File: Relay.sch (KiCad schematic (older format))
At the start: 11 parts

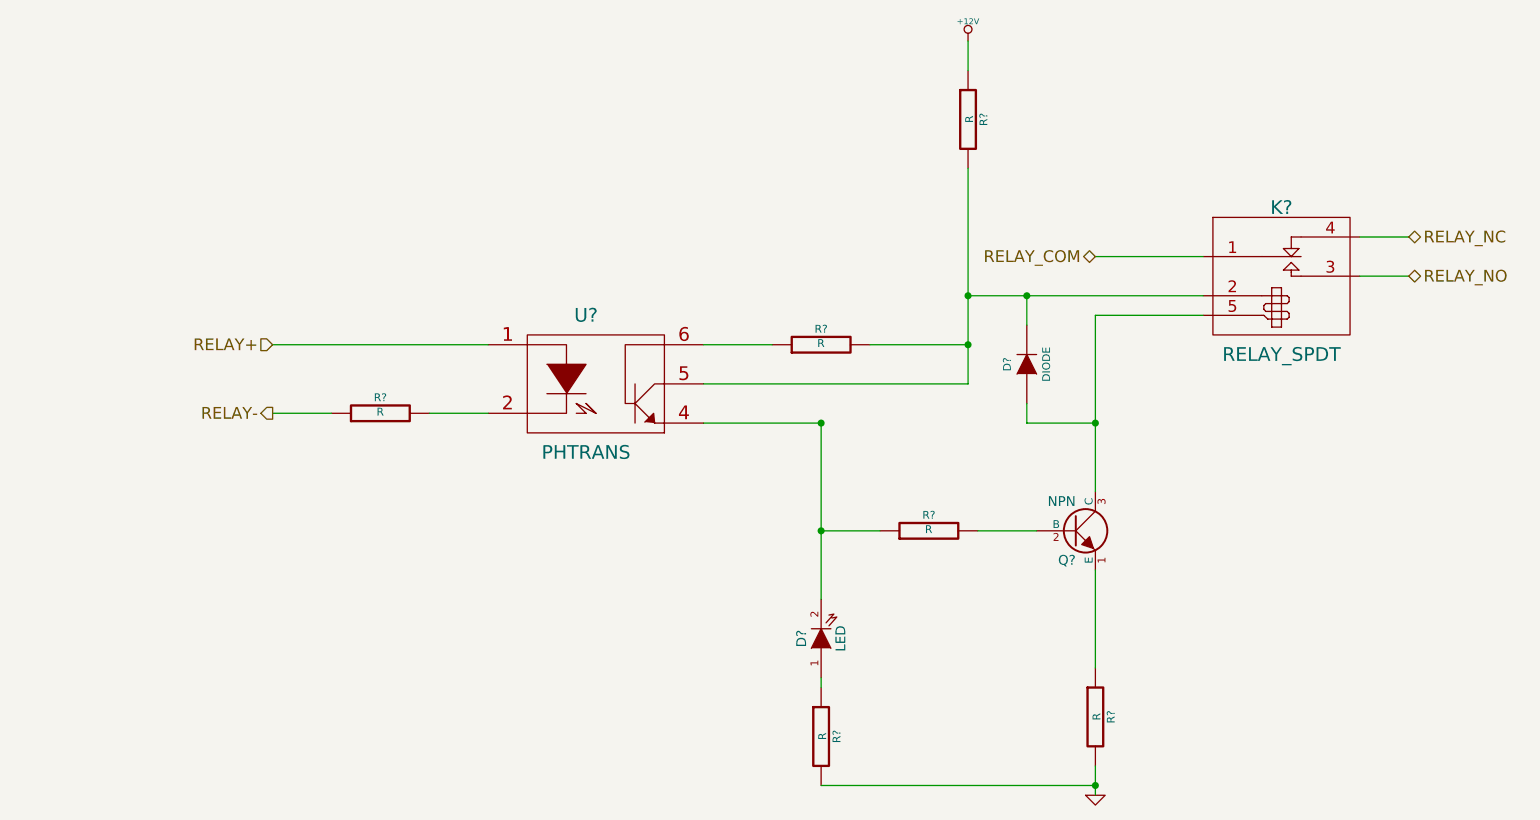
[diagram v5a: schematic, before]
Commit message: Begin Associating relay Module
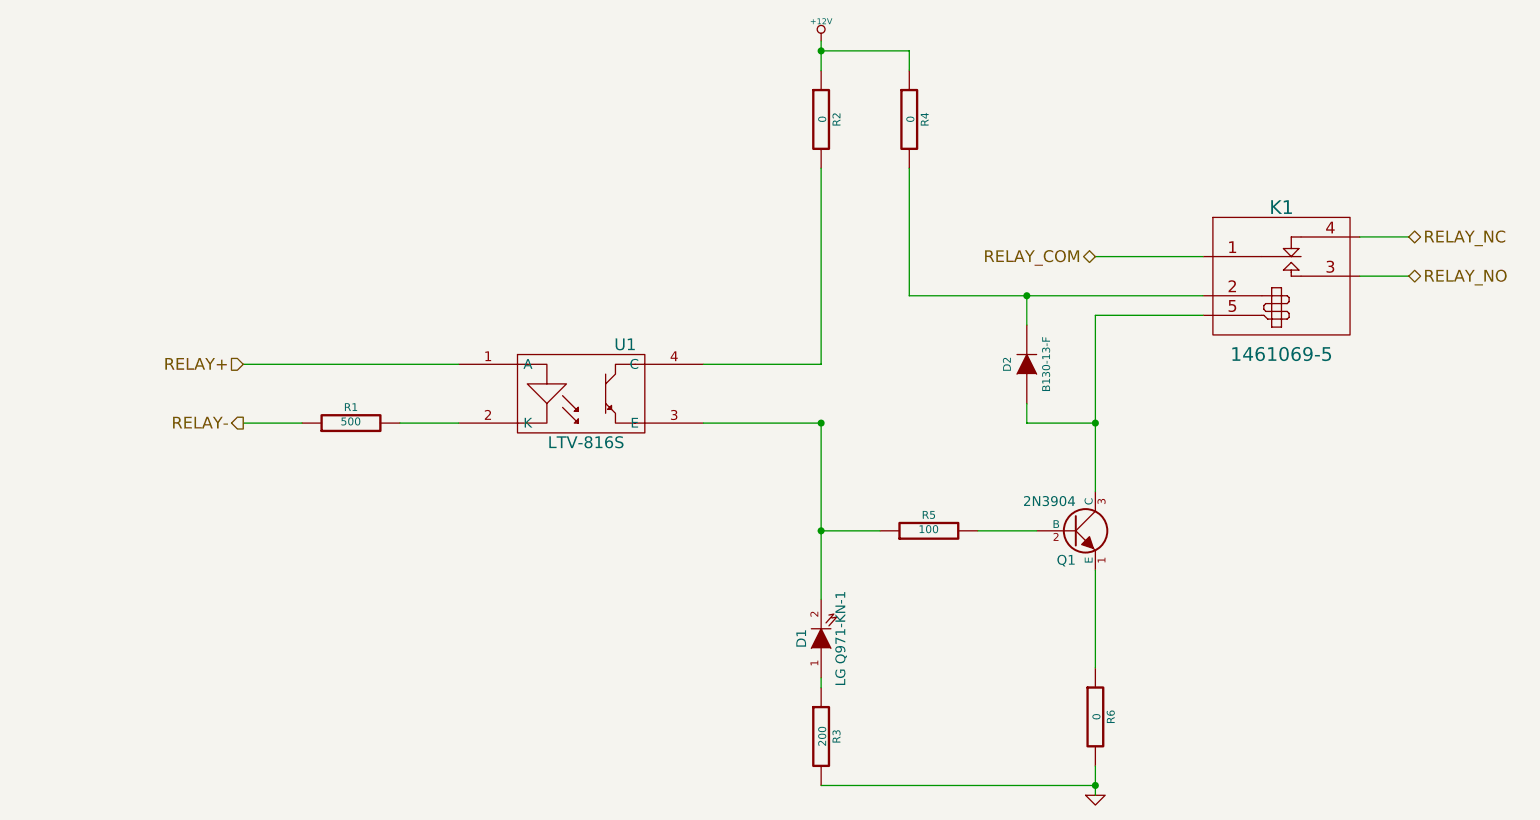
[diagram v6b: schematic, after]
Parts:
- removed R?: R, ~, symbol R
- removed U?: PHTRANS, ~, symbol PHTRANS
- added R4: 0, ~, symbol R
- added U1: LTV-816S, symbol OPTO-TRANSISTOR4
- D1: renamed from D?; value LED -> LG Q971-KN-1; MFG Part Number (none) -> LG Q971-KN-1
- D2: renamed from D?; value DIODE -> B130-13-F
- K1: renamed from K?; value RELAY_SPDT -> 1461069-5
- Q1: renamed from Q?; value NPN -> 2N3904; MFG Name (none) -> Diodes Inc; MFG Part Number (none) -> MMBT3904-7-F
- R1: renamed from R?; value R -> 500
- R2, R6: renamed from R?; value R -> 0
- R3: renamed from R?; value R -> 200
- R5: renamed from R?; value R -> 100
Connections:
- net +12V: now also R4.1
- net RELAY+: now also U1.1 (A)
- net at R1.2: now also U1.2 (K)
- net at D1.2 (K), R5.1: now also U1.3 (E)
- net at D2.2 (K), K1.2 (Coil+): now also R4.2; no longer R2.2
- new net: R2.2, U1.4 (C)
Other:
- moved on the sheet: R1, R2
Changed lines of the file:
@@
 LIBS:BenchBudEE
 LIBS:BenchBudEE-cache
-EELAYER 27 0
+EELAYER 24 0
 EELAYER END
 $Descr A4 11693 8268
 encoding utf-8
-Sheet 4 9
+Sheet 3 9
 Title ""
 Date "4 feb 2014"
@@
 Comment4 ""
 $EndDescr
-Text HLabel 3400 3400 0    60   Input ~ 0
+Text HLabel 3250 3500 0    60   Input ~ 0
 RELAY+
-Text HLabel 3400 3750 0    60   Output ~ 0
+Text HLabel 3250 3800 0    60   Output ~ 0
 RELAY-
 Text HLabel 9200 3050 2    60   BiDi ~ 0
@@
 RELAY_NC
 $Comp
-L PHTRANS U?
-U 1 1 52EFBD6E
-P 5050 3600
-F 0 "U?" H 5000 3950 70  0000 C CNN
-F 1 "PHTRANS" H 5000 3250 70  0000 C CNN
-F 2 "~" H 5050 3600 60  0000 C CNN
-F 3 "~" H 5050 3600 60  0000 C CNN
-	1    5050 3600
-	1    0    0    -1
-$EndComp
-$Comp
-L R R?
+L R R5
 U 1 1 52EFBD7D
 P 6750 4350
-F 0 "R?" V 6830 4350 40  0000 C CNN
-F 1 "R" V 6757 4351 40  0000 C CNN
+F 0 "R5" V 6830 4350 40  0000 C CNN
+F 1 "100" V 6757 4351 40  0000 C CNN
 F 2 "~" V 6680 4350 30  0000 C CNN
 F 3 "~" H 6750 4350 30  0000 C CNN
@@
 $EndComp
 $Comp
-L NPN Q?
+L NPN Q1
 U 1 1 52EFBDE3
 P 7500 4350
-F 0 "Q?" H 7500 4200 50  0000 R CNN
-F 1 "NPN" H 7500 4500 50  0000 R CNN
+F 0 "Q1" H 7500 4200 50  0000 R CNN
+F 1 "2N3904" H 7500 4500 50  0000 R CNN
 F 2 "~" H 7500 4350 60  0000 C CNN
 F 3 "~" H 7500 4350 60  0000 C CNN
+F 4 "Diodes Inc" H 7500 4350 60  0001 C CNN "MFG Name"
+F 5 "MMBT3904-7-F" H 7500 4350 60  0001 C CNN "MFG Part Number"
 	1    7500 4350
 	1    0    0    -1
 $EndComp
 $Comp
-L LED D?
+L LED D1
 U 1 1 52EFBDF2
 P 6200 4900
-F 0 "D?" H 6200 5000 50  0000 C CNN
-F 1 "LED" H 6200 4800 50  0000 C CNN
+F 0 "D1" H 6200 5000 50  0000 C CNN
+F 1 "LG Q971-KN-1" H 6200 4800 50  0000 C CNN
 F 2 "~" H 6200 4900 60  0000 C CNN
 F 3 "~" H 6200 4900 60  0000 C CNN
+F 4 "LG Q971-KN-1" H 6200 4900 60  0001 C CNN "MFG Part Number"
 	1    6200 4900
 	0    -1   -1   0
 $EndComp
 $Comp
-L RELAY_SPDT K?
+L RELAY_SPDT K1
 U 1 1 52EFC34C
 P 8550 2900
-F 0 "K?" H 8550 3100 70  0000 C CNN
-F 1 "RELAY_SPDT" H 8550 2350 70  0000 C CNN
+F 0 "K1" H 8550 3100 70  0000 C CNN
+F 1 "1461069-5" H 8550 2350 70  0000 C CNN
 F 2 "~" H 8550 2900 60  0000 C CNN
 F 3 "~" H 8550 2900 60  0000 C CNN
@@
 	7000 4350 7300 4350
 Wire Wire Line
-	7600 4150 7600 3250
+	7600 3250 7600 4150
 Wire Wire Line
 	7600 3250 8150 3250
 Wire Wire Line
-	8150 3150 6950 3150
-Wire Wire Line
-	6950 2500 6950 3600
-$Comp
-L R R?
+	6650 3150 8150 3150
+Wire Wire Line
+	6200 2500 6200 3500
+$Comp
+L R R6
 U 1 1 52EFC3AD
 P 7600 5300
-F 0 "R?" V 7680 5300 40  0000 C CNN
-F 1 "R" V 7607 5301 40  0000 C CNN
+F 0 "R6" V 7680 5300 40  0000 C CNN
+F 1 "0" V 7607 5301 40  0000 C CNN
 F 2 "~" V 7530 5300 30  0000 C CNN
 F 3 "~" H 7600 5300 30  0000 C CNN
@@
 	7600 4550 7600 5050
 $Comp
-L GND #PWR?
+L GND #PWR12
 U 1 1 52EFC3D1
 P 7600 5700
-F 0 "#PWR?" H 7600 5700 30  0001 C CNN
+F 0 "#PWR12" H 7600 5700 30  0001 C CNN
 F 1 "GND" H 7600 5630 30  0001 C CNN
 F 2 "" H 7600 5700 60  0000 C CNN
@@
 	7600 5550 7600 5700
 $Comp
-L R R?
+L R R3
 U 1 1 52EFC3F3
 P 6200 5400
-F 0 "R?" V 6280 5400 40  0000 C CNN
-F 1 "R" V 6207 5401 40  0000 C CNN
+F 0 "R3" V 6280 5400 40  0000 C CNN
+F 1 "200" V 6207 5401 40  0000 C CNN
 F 2 "~" V 6130 5400 30  0000 C CNN
 F 3 "~" H 6200 5400 30  0000 C CNN
@@
 Connection ~ 7600 5650
 $Comp
-L R R?
+L R R2
 U 1 1 52EFC424
-P 6950 2250
-F 0 "R?" V 7030 2250 40  0000 C CNN
-F 1 "R" V 6957 2251 40  0000 C CNN
-F 2 "~" V 6880 2250 30  0000 C CNN
-F 3 "~" H 6950 2250 30  0000 C CNN
-	1    6950 2250
-	1    0    0    -1
-$EndComp
-$Comp
-L +12V #PWR?
+P 6200 2250
+F 0 "R2" V 6280 2250 40  0000 C CNN
+F 1 "0" V 6207 2251 40  0000 C CNN
+F 2 "~" V 6130 2250 30  0000 C CNN
+F 3 "~" H 6200 2250 30  0000 C CNN
+	1    6200 2250
+	1    0    0    -1
+$EndComp
+$Comp
+L +12V #PWR11
 U 1 1 52EFC433
-P 6950 1850
-F 0 "#PWR?" H 6950 1800 20  0001 C CNN
-F 1 "+12V" H 6950 1950 30  0000 C CNN
-F 2 "" H 6950 1850 60  0000 C CNN
-F 3 "" H 6950 1850 60  0000 C CNN
-	1    6950 1850
-	1    0    0    -1
-$EndComp
-Wire Wire Line
-	6950 1850 6950 2000
-Wire Wire Line
-	6950 3600 5600 3600
-Connection ~ 6950 3150
-$Comp
-L R R?
-U 1 1 52EFC463
-P 6200 3400
-F 0 "R?" V 6280 3400 40  0000 C CNN
-F 1 "R" V 6207 3401 40  0000 C CNN
-F 2 "~" V 6130 3400 30  0000 C CNN
-F 3 "~" H 6200 3400 30  0000 C CNN
-	1    6200 3400
-	0    -1   -1   0
-$EndComp
-Wire Wire Line
-	5600 3400 5950 3400
-Wire Wire Line
-	6450 3400 6950 3400
-Connection ~ 6950 3400
-Wire Wire Line
-	3400 3400 4500 3400
-$Comp
-L R R?
+P 6200 1850
+F 0 "#PWR11" H 6200 1800 20  0001 C CNN
+F 1 "+12V" H 6200 1950 30  0000 C CNN
+F 2 "" H 6200 1850 60  0000 C CNN
+F 3 "" H 6200 1850 60  0000 C CNN
+	1    6200 1850
+	1    0    0    -1
+$EndComp
+Wire Wire Line
+	6200 1850 6200 2000
+Wire Wire Line
+	6200 3500 5600 3500
+Wire Wire Line
+	3250 3500 4350 3500
+$Comp
+L R R1
 U 1 1 52EFC4A9
-P 3950 3750
-F 0 "R?" V 4030 3750 40  0000 C CNN
-F 1 "R" V 3957 3751 40  0000 C CNN
-F 2 "~" V 3880 3750 30  0000 C CNN
-F 3 "~" H 3950 3750 30  0000 C CNN
-	1    3950 3750
-	0    -1   -1   0
-$EndComp
-Wire Wire Line
-	3400 3750 3700 3750
-Wire Wire Line
-	4200 3750 4500 3750
-$Comp
-L DIODE D?
+P 3800 3800
+F 0 "R1" V 3880 3800 40  0000 C CNN
+F 1 "500" V 3807 3801 40  0000 C CNN
+F 2 "~" V 3730 3800 30  0000 C CNN
+F 3 "~" H 3800 3800 30  0000 C CNN
+	1    3800 3800
+	0    -1   -1   0
+$EndComp
+Wire Wire Line
+	3250 3800 3550 3800
+Wire Wire Line
+	4050 3800 4350 3800
+$Comp
+L DIODE D2
 U 1 1 52EFC4E6
 P 7250 3500
-F 0 "D?" H 7250 3600 40  0000 C CNN
-F 1 "DIODE" H 7250 3400 40  0000 C CNN
+F 0 "D2" H 7250 3600 40  0000 C CNN
+F 1 "B130-13-F" H 7250 3400 40  0000 C CNN
 F 2 "~" H 7250 3500 60  0000 C CNN
 F 3 "~" H 7250 3500 60  0000 C CNN
@@
 	6500 4350 6200 4350
 Connection ~ 6200 4350
+$Comp
+L OPTO-TRANSISTOR4 U1
+U 1 1 5302908A
+P 5000 3650
+F 0 "U1" H 5200 3900 60  0000 C CNN
+F 1 "LTV-816S" H 5000 3400 60  0000 C CNN
+F 2 "" H 5000 3650 60  0000 C CNN
+F 3 "" H 5000 3650 60  0000 C CNN
+F 4 "LTV-816S" H 5000 3650 60  0001 C CNN "MFG Part Number"
+	1    5000 3650
+	1    0    0    -1
+$EndComp
+$Comp
+L R R4
+U 1 1 530291BA
+P 6650 2250
+F 0 "R4" V 6730 2250 40  0000 C CNN
+F 1 "0" V 6657 2251 40  0000 C CNN
+F 2 "~" V 6580 2250 30  0000 C CNN
+F 3 "~" H 6650 2250 30  0000 C CNN
+	1    6650 2250
+	1    0    0    -1
+$EndComp
+Wire Wire Line
+	6650 2000 6650 1900
+Wire Wire Line
+	6650 1900 6200 1900
+Connection ~ 6200 1900
+Wire Wire Line
+	6650 3150 6650 2500
 $EndSCHEMATC
